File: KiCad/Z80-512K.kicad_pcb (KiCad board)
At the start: 2 copper layers, 99.1 x 49.9 mm, 32 parts, among them J1 VBAT, J2 JTAG, J3 RC2014_BUS, J4 RC2014_EXT, U1 Z84C00, U2 SST39SF040, U3 AS6C4008, U4 ATF1504AS, U5 ADM693A, X1 7.3728MHz

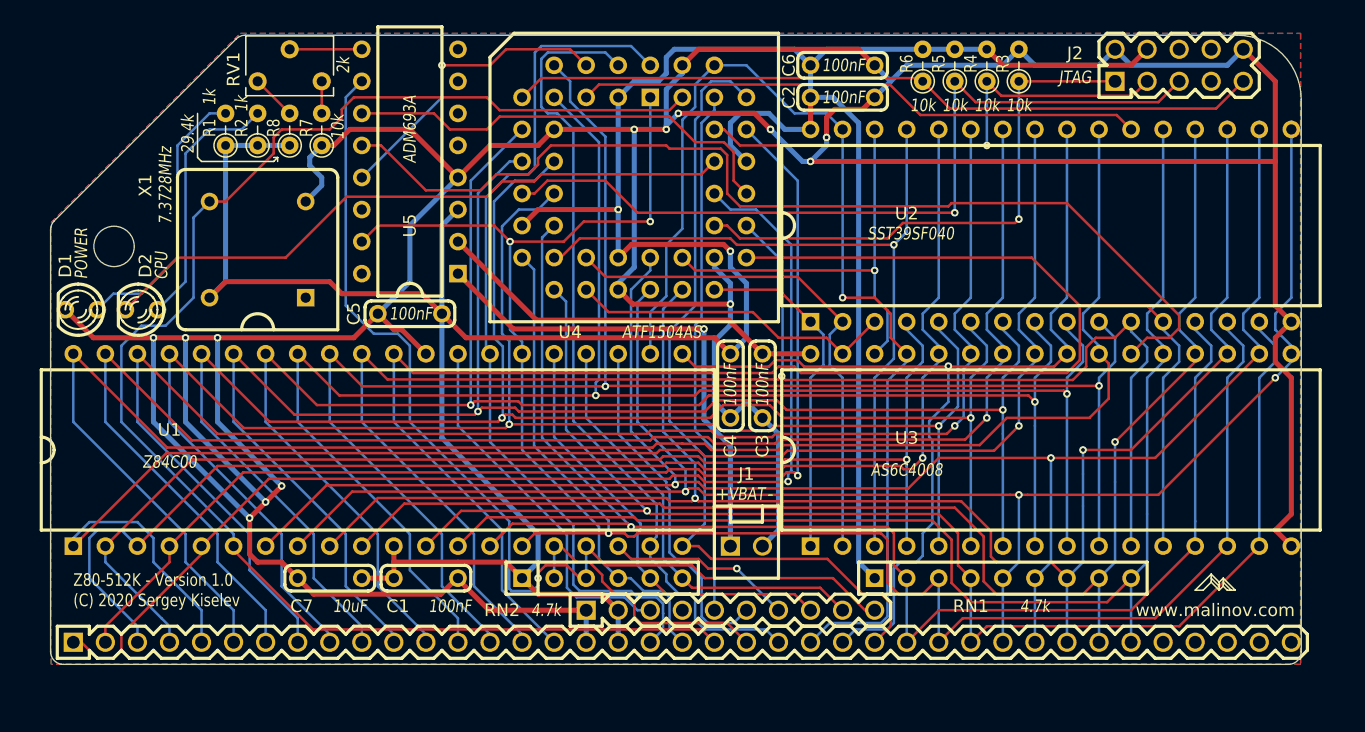
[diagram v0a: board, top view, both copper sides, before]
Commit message: Update KiCad, gerber, and README for Version 1.1
Signed-off-by: Sergey Kiselev <skiselev@gmail.com>
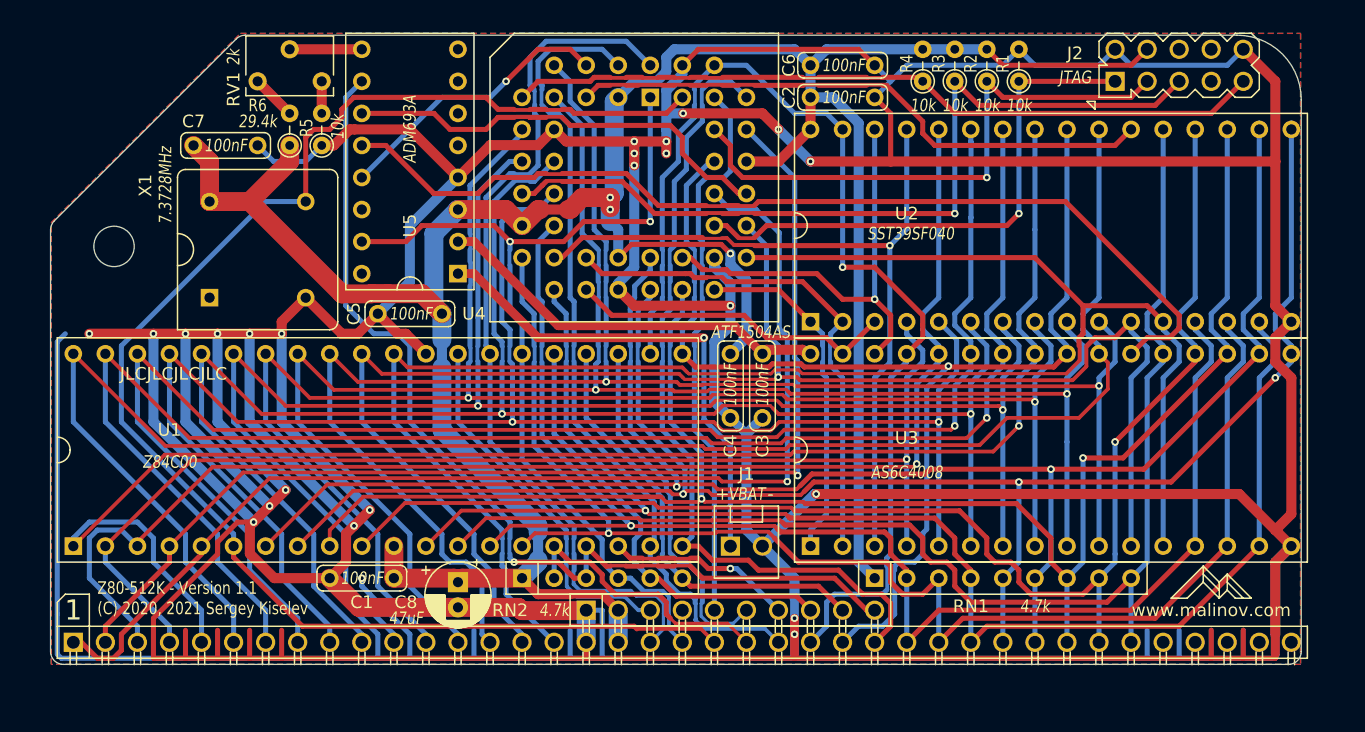
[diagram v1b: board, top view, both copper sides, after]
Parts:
- removed D1: POWER, My_Components:LED_3mm
- removed D2: CPU, My_Components:LED_3mm
- removed the R1 at (139.1, 87.6)
- removed the R2 at (141.6, 87.6)
- removed R8: 29.4k, Resistor_THT:R_Axial_DIN0204_L3.6mm_D1.6mm_P2.54mm_Vertical
- removed the REF** at (204.5, 96.8)
- added C8: 47uF, Capacitor_THT:CP_Radial_D5.0mm_P2.00mm, F.Cu at (157.5, 122.2)
- added LOGO1: Logo_Open_Hardware_Small, Symbol:OSHW-Logo_5.7x6mm_SilkScreen, B.Cu at (216.2, 94.9)
- added R6: 29.4k, Resistor_THT:R_Axial_DIN0204_L3.6mm_D1.6mm_P2.54mm_Vertical, F.Cu at (144.1, 87.6)
- added REF**: KiCad-Logo2_5mm_SilkScreen, Symbol:KiCad-Logo2_5mm_SilkScreen, B.Cu at (204.5, 111.4)
- C7: value 10uF -> 100nF
- J3: footprint My_Components:Conn_Pin_Header_39x1_2.54mm -> My_Components:Conn_Pin_Header_39x1_2.54mm_Right_Angle
- J4: footprint My_Components:Conn_Pin_Header_10x1_2.54mm -> My_Components:Conn_Pin_Header_10x1_2.54mm_Right_Angle
- U1: footprint My_Components:IC_DIP40_600 -> My_Components:Socket_DIP40_600
- U2, U3: footprint My_Components:IC_DIP32_600 -> My_Components:Socket_DIP32_600
- U5: footprint My_Components:IC_DIP16_300 -> My_Components:Socket_DIP16_300
- moved C7 35.3 mm to (139.1, 87.6), turned to 0 degrees
- moved C1 5.08 mm to (149.9, 121.9), turned to 180 degrees
- turned X1 to 0 degrees
- renumbered R3 to R1, R4 to R2, R5 to R3, R6 to R4, R7 to R5
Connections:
- U4 pad 36: /LED_OUT -> /~RD
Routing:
- net GND: track 377.6 -> 787.7 mm, vias 13 -> 24
- net /LED_OUT: track 51.5 -> 0.00 mm
- net Net-(D1-Pad2): track 21.8 -> 0.00 mm
- net Net-(D2-Pad2): track 20.3 -> 0.00 mm
- net /TDI: track 59.7 -> 78.1 mm
- net VCC: track 265.2 -> 247.2 mm, vias 2 -> 3
- net /~RD: track 78.4 -> 95.5 mm
- net /D5: track 132.0 -> 147.9 mm
- net /D3: track 135.5 -> 150.2 mm
- net /MA17: track 34.3 -> 48.8 mm
- net /MA14: track 61.8 -> 75.0 mm
- net /D4: track 140.1 -> 153.3 mm
- net /A4: track 133.9 -> 144.2 mm
- net /TMS: track 65.3 -> 71.7 mm
- net /~ROM_CS: track 45.1 -> 49.8 mm
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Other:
- rule pad_to_mask_clearance: 0.051 -> 0
- board text added: "!"
- board text added: "1"
- board text added: "A0"
- board text added: "A1"
- board text added: "A10"
- board text added: "A11"
- board text added: "A12"
- board text added: "A13"
- board text added: "A14"
- board text added: "A15"
- board text added: "A2"
- board text added: "A3"
- board text added: "A4"
- board text added: "A5"
- board text added: "A6"
- board text added: "A7"
- board text added: "A8"
- board text added: "A9"
- board text added: "Connect 3V battery to J1 for battery-backed SRAM Place a jumper over J1 if battery backup is not required"
- board text added: "D0"
- board text added: "D1"
- board text added: "D2"
- board text added: "D3"
- board text added: "D4"
- board text added: "D5"
- board text added: "D6"
- board text added: "D7"
- board text added: "Design files and documentation: github.com/skiselev/Z80-512K"
- board text added: "GND"
- board text added: "JLCJLCJLCJLC"
- board text added: "Licensed under CERN-OHL-S: https://cern-ohl.web.cern.ch"
- board text added: "M1"
- board text added: "RXDA"
- board text added: "TCK"
- board text added: "TDI"
- board text added: "TDO"
- board text added: "TMS"
- board text added: "TXDA"
- board text added: "USR1"
- board text added: "USR2"
- board text added: "USR3"
- board text added: "VCC"
- board text added: "Z80-512K - Version 1.1 (C) 2020, 2021 Sergey Kiselev"
- board text added: "Z80-512K - Version 1.1 Copyright (C) 2020, 2021 Sergey Kiselev"
- board text added: "~BACK"
- board text added: "~BREQ"
- board text added: "~CLK1"
- board text added: "~CLK2"
- board text added: "~HALT"
- board text added: "~INT"
- board text added: "~IORQ"
- board text added: "~MREQ"
- board text added: "~NMI"
- board text added: "~RD"
- board text added: "~RESET"
- board text added: "~RFSH"
- board text added: "~WAIT"
- board text added: "~WR"
- board text removed: "Z80-512K - Version 1.0 (C) 2020 Sergey Kiselev"
- board text removed: "Z80-512K - Version 1.0 Copyright (C) 2020 Sergey Kiselev"

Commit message: Replace design files with version 1.2. Update README accordingly
Signed-off-by: Sergey Kiselev <skiselev@gmail.com>
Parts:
- added D1: CPU, My_Components:LED_3mm, F.Cu at (128.3, 100.3)
- added R7: 1k, Resistor_THT:R_Axial_DIN0204_L3.6mm_D1.6mm_P2.54mm_Vertical, F.Cu at (133.3, 101.6)
- moved REF** 3.93 mm to (200.7, 112.4)
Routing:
- net GND: track 787.7 -> 842.0 mm, vias 24 -> 27
- net /WDOG: track 39.7 -> 71.5 mm
- net VCC: track 247.2 -> 258.5 mm
- net Net-(D1-Pad2): track 0.00 -> 4.34 mm
- net /~RAM_CSI: track 22.5 -> 25.7 mm
- net /~NMI: track 79.2 -> 81.0 mm
- net /CPU_CLK: track 121.0 -> 121.7 mm
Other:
- board text added: "Designed in Oregon"
- board text added: "Z80-512K - Version 1.2 (C) 2020, 2021 Sergey Kiselev"
- board text added: "Z80-512K - Version 1.2 Copyright (C) 2020, 2021 Sergey Kiselev"
- board text removed: "Z80-512K - Version 1.1 (C) 2020, 2021 Sergey Kiselev"
- board text removed: "Z80-512K - Version 1.1 Copyright (C) 2020, 2021 Sergey Kiselev"

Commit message: Update files for V2.0
Signed-off-by: Sergey Kiselev <skiselev@gmail.com>
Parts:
- removed C8: 47uF, Capacitor_THT:CP_Radial_D5.0mm_P2.00mm
- removed J4: RC2014_EXT, My_Components:Conn_Pin_Header_10x1_2.54mm_Right_Angle
- C1: value 100nF -> 10uF
- J1: footprint My_Components:Conn_Friction_Lock_2P_2.54mm -> Connector_PinHeader_2.54mm:PinHeader_1x02_P2.54mm_Horizontal
- J3: value RC2014_BUS -> RCBus-80; footprint My_Components:Conn_Pin_Header_39x1_2.54mm_Right_Angle -> My_Components:Conn_Pin_Header_40x2_2.54mm_Right_Angle_RCBus80
- moved J1 55.3 mm to (133.3, 90.2), turned to 180 degrees
- moved D1 17.7 mm to (134.6, 83.8)
- moved R7 17.5 mm to (139.1, 85.1), turned to 0 degrees
- moved J3 1.27 mm to (175.3, 128.3)
- moved H1 1.06 mm to (130.8, 96.5)
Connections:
- net /~INT renamed /~{INT}
- net /~IORQ renamed /~{IORQ}
- net /~M1 renamed /~{M1}
- net /~MREQ renamed /~{MREQ}
- net /~RAM_CS renamed /~{RAM_CS}
- net /~RAM_CSI renamed /~{RAM_CSI}
- net /~RD renamed /~{RD}
- net /~RESET renamed /~{RESET}
- net /~ROM_CS renamed /~{ROM_CS}
- net /~WR renamed /~{WR}
- J2 pad 6: Net-(J2-Pad6) -> unconnected-(J2-Pad6)
- J2 pad 7: Net-(J2-Pad7) -> unconnected-(J2-Pad7)
- J2 pad 8: Net-(J2-Pad8) -> unconnected-(J2-Pad8)
- J3 pad 35: /TXDA -> unconnected-(J3-Pad35)
- J3 pad 36: /RXDA -> unconnected-(J3-Pad36)
- J3 pad 37: /USR1 -> unconnected-(J3-Pad37)
- J3 pad 38: /USR2 -> unconnected-(J3-Pad38)
- J3 pad 39: /USR3 -> unconnected-(J3-Pad39)
- R7 pad 1: VCC -> Net-(D1-Pad2)
- R7 pad 2: Net-(D1-Pad2) -> VCC
- RN2 pad 3: /~NMI -> /~{NMI}
- RN2 pad 5: /~BUSREQ -> /~{BUSREQ}
- RN2 pad 6: /~WAIT -> /~{WAIT}
- U1 pad 17: /~NMI -> /~{NMI}
- U1 pad 18: /~HALT -> /~{HALT}
- U1 pad 23: /~BUSACK -> /~{BUSACK}
- U1 pad 24: /~WAIT -> /~{WAIT}
- U1 pad 25: /~BUSREQ -> /~{BUSREQ}
- U1 pad 28: /~RFSH -> /~{RFSH}
- U5 pad 10: /~NMI -> /~{NMI}
- U5 pad 14: Net-(U5-Pad14) -> unconnected-(U5-Pad14)
- U5 pad 16: Net-(U5-Pad16) -> unconnected-(U5-Pad16)
- U5 pad 5: Net-(U5-Pad5) -> unconnected-(U5-Pad5)
- U5 pad 6: Net-(U5-Pad6) -> unconnected-(U5-Pad6)
- U5 pad 7: Net-(U5-Pad7) -> unconnected-(U5-Pad7)
- U5 pad 8: Net-(U5-Pad8) -> unconnected-(U5-Pad8)
- X1 pad 1: Net-(X1-Pad1) -> unconnected-(X1-Pad1)
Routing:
- net GND: track 842.0 -> 694.4 mm, vias 27 -> 34
- net /~{NMI}: track 0.00 -> 81.5 mm, vias 0 -> 1
- net /~NMI: track 81.0 -> 0.00 mm, vias 1 -> 0
- net /~{BUSREQ}: track 0.00 -> 36.0 mm
- net /~{WAIT}: track 0.00 -> 35.3 mm
- net /~BUSREQ: track 35.1 -> 0.00 mm
- net /~WAIT: track 34.8 -> 0.00 mm
- net /~{RFSH}: track 0.00 -> 30.1 mm
- net /~{BUSACK}: track 0.00 -> 29.5 mm
- net /~RFSH: track 29.4 -> 0.00 mm
- net /~BUSACK: track 28.2 -> 0.00 mm
- net VCC: track 258.5 -> 240.1 mm
- net /~{HALT}: track 0.00 -> 15.4 mm, vias 0 -> 1
- net /~HALT: track 14.9 -> 0.00 mm, vias 1 -> 0
- net /WDOG: track 71.5 -> 57.8 mm
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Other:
- board size 99.1 x 49.9 mm -> 101.6 x 53.3 mm
- net class Default removed
- net class Power removed
- board text added: "Install jumpers w/o ADM693A"
- board text added: "RCBus Z80 CPU, 512 KiB SRAM and 512 KiB Flash ROM Module"
- board text added: "SK105"
- board text added: "U5, C5, R5, R6, RV1 and J1 are optional - required for on-board CPU supervisor and battery-backed SRAM Install wire jumpers as indicated if not using this feature Connect 3V battery to J1 for battery-backed SRAM Place a jumper over J1 if battery backup is not required"
- board text added: "Z80-512K - Version 2.0 (C) 2020-2024 Sergey Kiselev"
- board text added: "Z80-512K - Version 2.0 Copyright (C) 2020 - 2024 Sergey Kiselev"
- board text removed: "1"
- board text removed: "A0"
- board text removed: "A1"
- board text removed: "A10"
- board text removed: "A11"
- board text removed: "A12"
- board text removed: "A13"
- board text removed: "A14"
- board text removed: "A15"
- board text removed: "A2"
- board text removed: "A3"
- board text removed: "A4"
- board text removed: "A5"
- board text removed: "A6"
- board text removed: "A7"
- board text removed: "A8"
- board text removed: "A9"
- board text removed: "Connect 3V battery to J1 for battery-backed SRAM Place a jumper over J1 if battery backup is not required"
- board text removed: "D0"
- board text removed: "D1"
- board text removed: "D2"
- board text removed: "D3"
- board text removed: "D4"
- board text removed: "D5"
- board text removed: "D6"
- board text removed: "D7"
- board text removed: "M1"
- board text removed: "RXDA"
- board text removed: "TXDA"
- board text removed: "USR1"
- board text removed: "USR2"
- board text removed: "USR3"
- board text removed: "Z80-512K - Version 1.2 (C) 2020, 2021 Sergey Kiselev"
- board text removed: "Z80-512K - Version 1.2 Copyright (C) 2020, 2021 Sergey Kiselev"
- board text removed: "~BACK"
- board text removed: "~BREQ"
- board text removed: "~CLK1"
- board text removed: "~CLK2"
- board text removed: "~HALT"
- board text removed: "~INT"
- board text removed: "~IORQ"
- board text removed: "~MREQ"
- board text removed: "~NMI"
- board text removed: "~RD"
- board text removed: "~RESET"
- board text removed: "~RFSH"
- board text removed: "~WAIT"
- board text removed: "~WR"
